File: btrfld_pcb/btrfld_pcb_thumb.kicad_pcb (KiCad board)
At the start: 2 copper layers, 53.7 x 30.8 mm, 11 parts

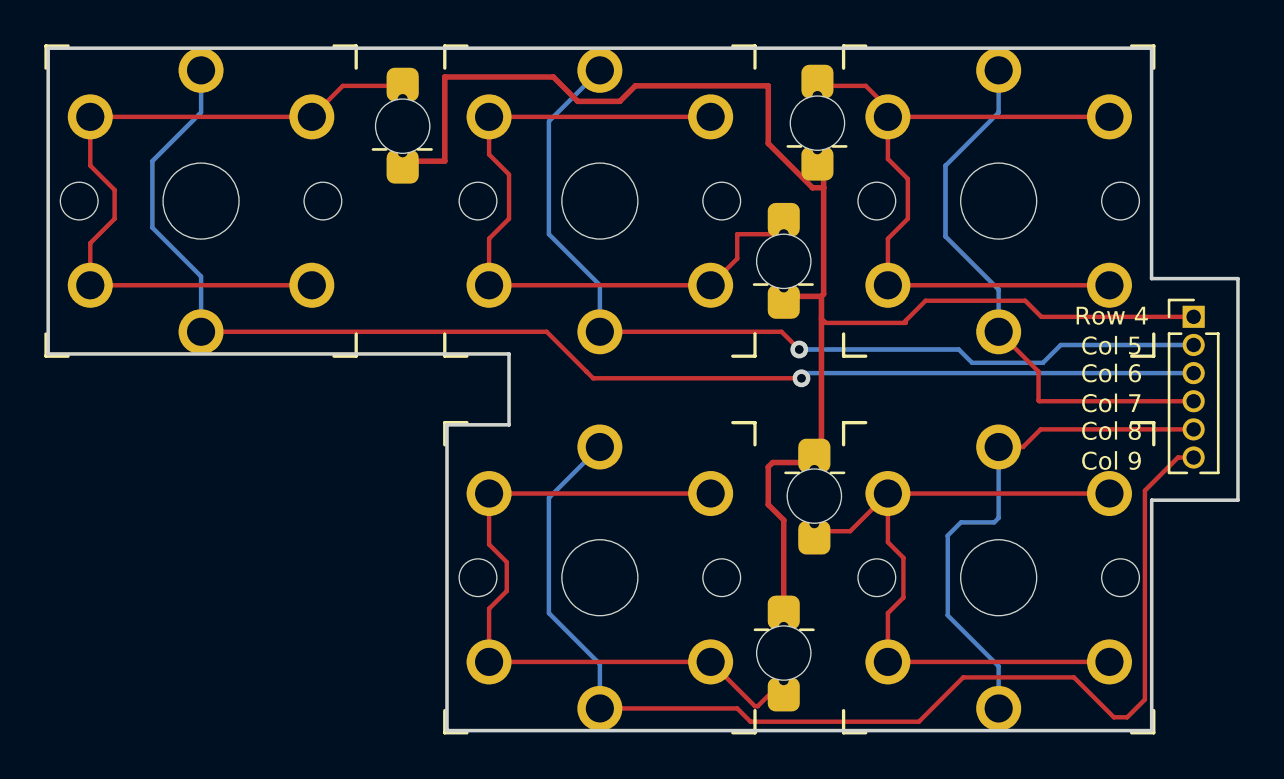
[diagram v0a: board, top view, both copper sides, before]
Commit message: fixup flipped diode holes so copper connects pads on either side of board
also fixup some tracing while we are at it
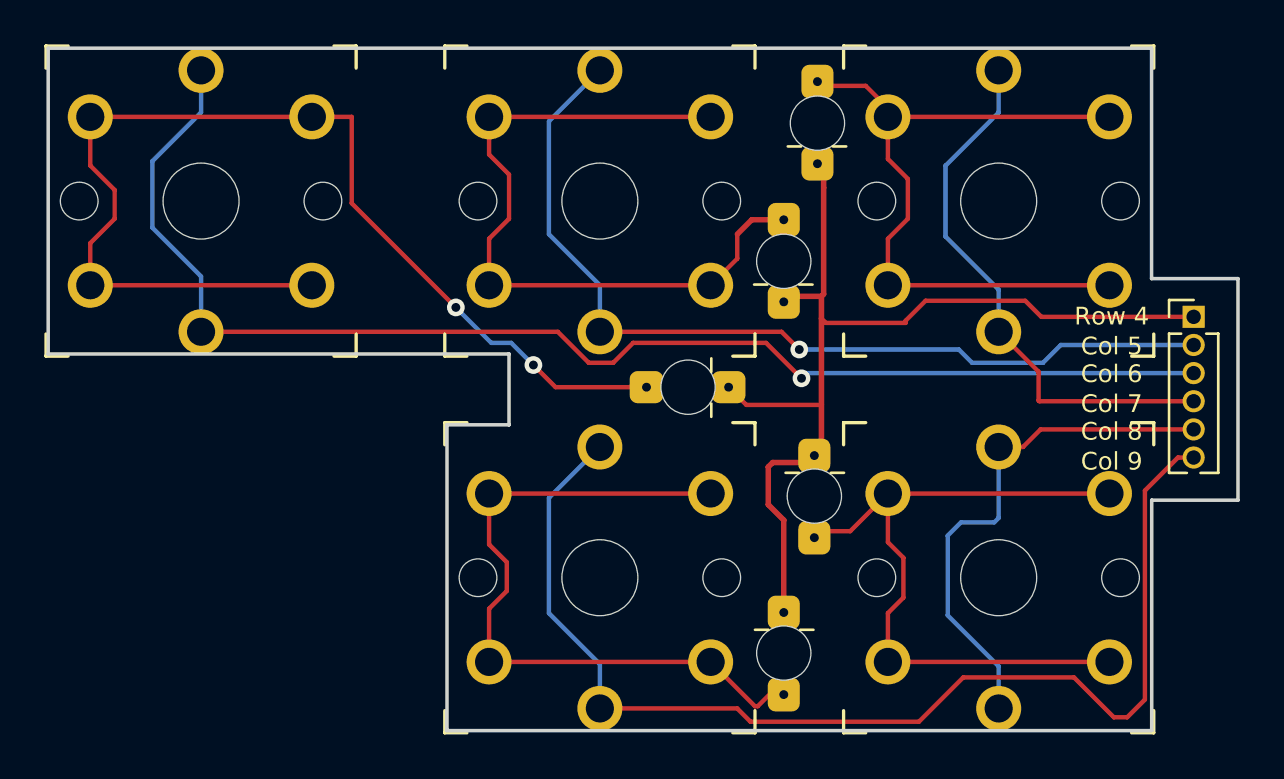
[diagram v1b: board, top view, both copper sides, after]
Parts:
- moved REF** 18.2 mm to (147.1, 97.9), turned to 90 degrees
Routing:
- net (no net): track 437.7 -> 433.6 mm, vias 2 -> 4
